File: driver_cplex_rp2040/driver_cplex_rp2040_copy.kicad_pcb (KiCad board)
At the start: 6 copper layers, 40.2 x 40.2 mm, 479 parts, among them J1 Conn_01x05, J2 Conn_01x05, J3 Conn_01x05, J4 Conn_01x05, J5 Conn_01x04, Q1 1xPNP and 1xNPN, Q10 1xPNP and 1xNPN, Q11 1xPNP and 1xNPN, Q12 1xPNP and 1xNPN, Q13 1xPNP and 1xNPN, Q14 1xPNP and 1xNPN, Q15 1xPNP and 1xNPN, Q16 1xPNP and 1xNPN, Q17 1xPNP and 1xNPN, Q18 1xPNP and 1xNPN, Q19 1xPNP and 1xNPN, Q2 1xPNP and 1xNPN, Q20 1xPNP and 1xNPN, Q21 1xPNP and 1xNPN, Q22 1xPNP and 1xNPN, Q23 1xPNP and 1xNPN, Q24 1xPNP and 1xNPN, Q25 1xPNP and 1xNPN, Q26 1xPNP and 1xNPN, Q27 1xPNP and 1xNPN, Q28 1xPNP and 1xNPN, Q29 1xPNP and 1xNPN, Q3 1xPNP and 1xNPN, Q30 1xPNP and 1xNPN, Q31 1xPNP and 1xNPN, Q32 1xPNP and 1xNPN, Q33 1xPNP and 1xNPN, Q34 1xPNP and 1xNPN, Q4 1xPNP and 1xNPN, Q5 1xPNP and 1xNPN, Q6 1xPNP and 1xNPN, Q7 1xPNP and 1xNPN, Q8 1xPNP and 1xNPN, Q9 1xPNP and 1xNPN, SW1 SW_Push, SW2 SW_Push, U1 AP2112K-3.3, U2 RP2040, U3 W25Q16JVUXIQ_TR, Y1 12MHz

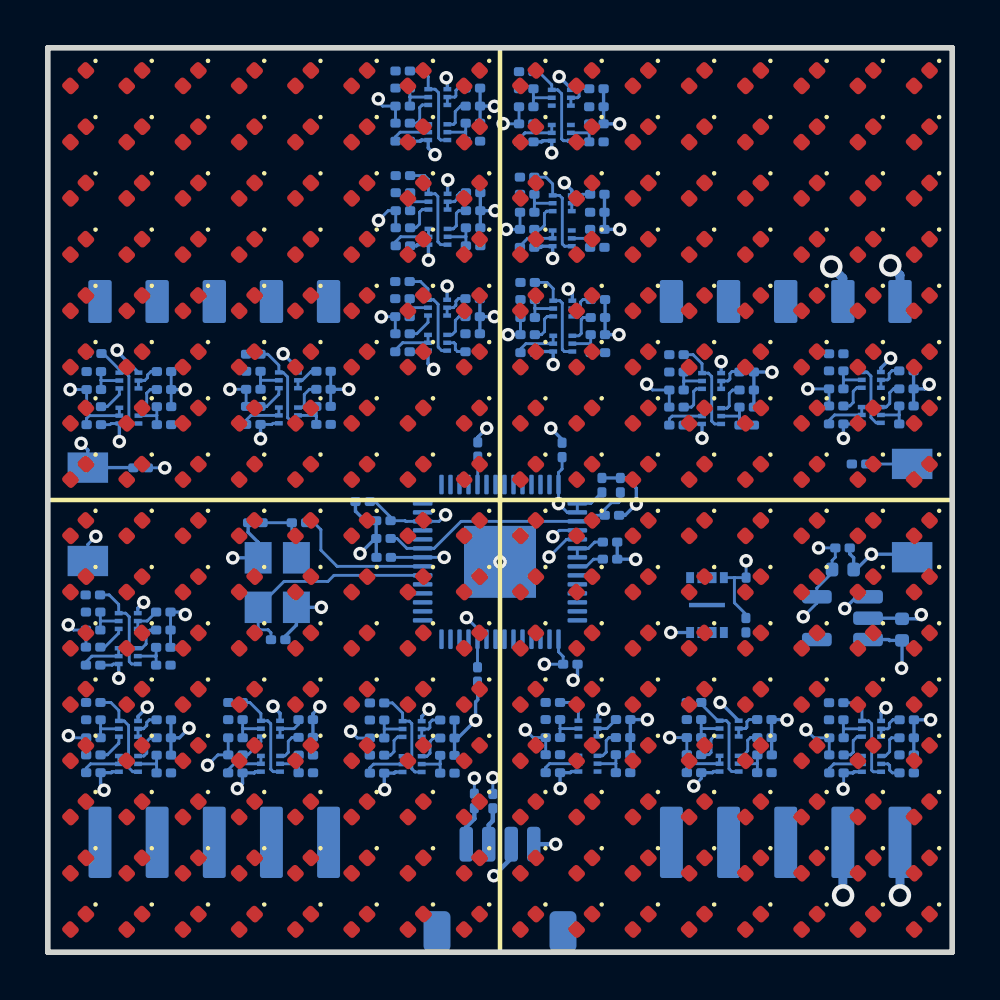
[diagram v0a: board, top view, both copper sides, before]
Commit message: Work on rp2040 cplex'd design routing and layout.
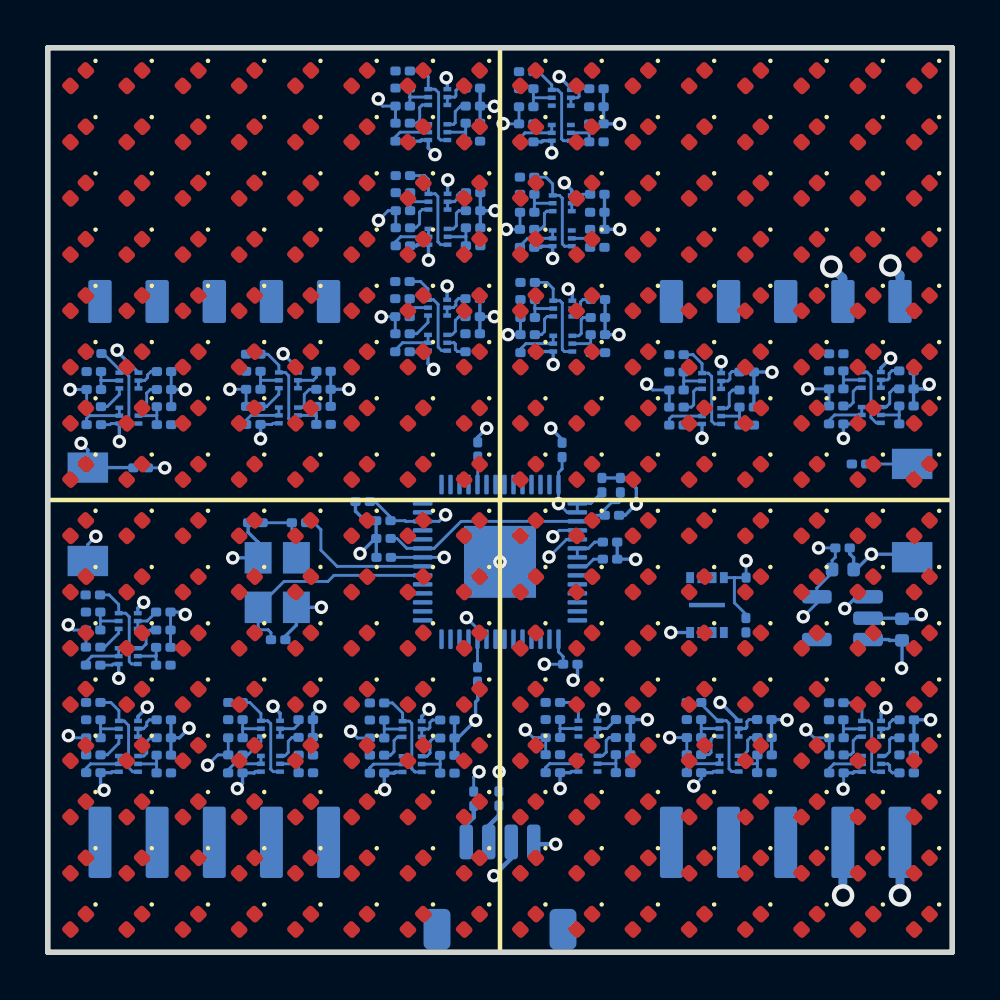
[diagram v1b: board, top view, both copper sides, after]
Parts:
- moved R1 0.29 mm to (70.0, 83.3)
- moved J5 0.10 mm to (70.0, 87.2)
- moved R2 0.10 mm to (68.8, 83.3)
